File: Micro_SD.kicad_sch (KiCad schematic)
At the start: 3 parts, among them J2 DM3BT-DSF-PEJS

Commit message: BOM update
completed the BOM list
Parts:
- C27: MANUFACTURER (none) -> Murata Electronics; MANUFACTURER_PART_NUMBER (none) -> GCM155R71H104KE02D
- C33: MANUFACTURER (none) -> Murata Electronics; MANUFACTURER_PART_NUMBER (none) -> GRT155R61A105KE01D
- J2: MANUFACTURER (none) -> Hirose Electric Co Ltd; MANUFACTURER_PART_NUMBER (none) -> DM3BT-DSF-PEJS
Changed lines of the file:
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@@
+			)
+		)
+		(property "MANUFACTURER" "Murata Electronics"
+			(at 113.03 92.71 0)
+			(effects
+				(font
+					(size 1.27 1.27)
+				)
+				(hide yes)
+			)
+		)
+		(property "MANUFACTURER_PART_NUMBER" "GCM155R71H104KE02D"
+			(at 113.03 92.71 0)
+			(effects
+				(font
+					(size 1.27 1.27)
+				)
+				(hide yes)
 			)
 		)
@@
 			)
 		)
+		(property "MANUFACTURER" "Hirose Electric Co Ltd"
+			(at 128.27 69.85 0)
+			(effects
+				(font
+					(size 1.27 1.27)
+				)
+				(hide yes)
+			)
+		)
+		(property "MANUFACTURER_PART_NUMBER" "DM3BT-DSF-PEJS"
+			(at 128.27 69.85 0)
+			(effects
+				(font
+					(size 1.27 1.27)
+				)
+				(hide yes)
+			)
+		)
 		(pin "6"
 		)
@@
 			(at 124.46 92.71 0)
 			(effects
+				(font
+					(size 1.27 1.27)
+				)
+				(hide yes)
+			)
+		)
+		(property "MANUFACTURER" "Murata Electronics"
+			(at 124.46 92.71 0)
+			(effects
+				(font
+					(size 1.27 1.27)
+				)
+				(hide yes)
+			)
+		)
+		(property "MANUFACTURER_PART_NUMBER" "GRT155R61A105KE01D"
+			(at 124.46 92.71 0)
+			(effects

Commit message: Made some minor adjustments
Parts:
- C27: footprint Capacitor_SMD:C_0402_1005Metric -> Capacitor_SMD:C_0603_1608Metric
- C33: footprint Capacitor_SMD:C_0402_1005Metric -> Capacitor_SMD:C_0805_2012Metric
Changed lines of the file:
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@@
 			)
 		)
-		(property "Footprint" "Capacitor_SMD:C_0402_1005Metric"
+		(property "Footprint" "Capacitor_SMD:C_0603_1608Metric"
 			(at 113.9952 96.52 0)
 			(effects
@@
 			)
 		)
-		(property "Footprint" "Capacitor_SMD:C_0402_1005Metric"
+		(property "Footprint" "Capacitor_SMD:C_0805_2012Metric"
 			(at 125.4252 96.52 0)
 			(effects

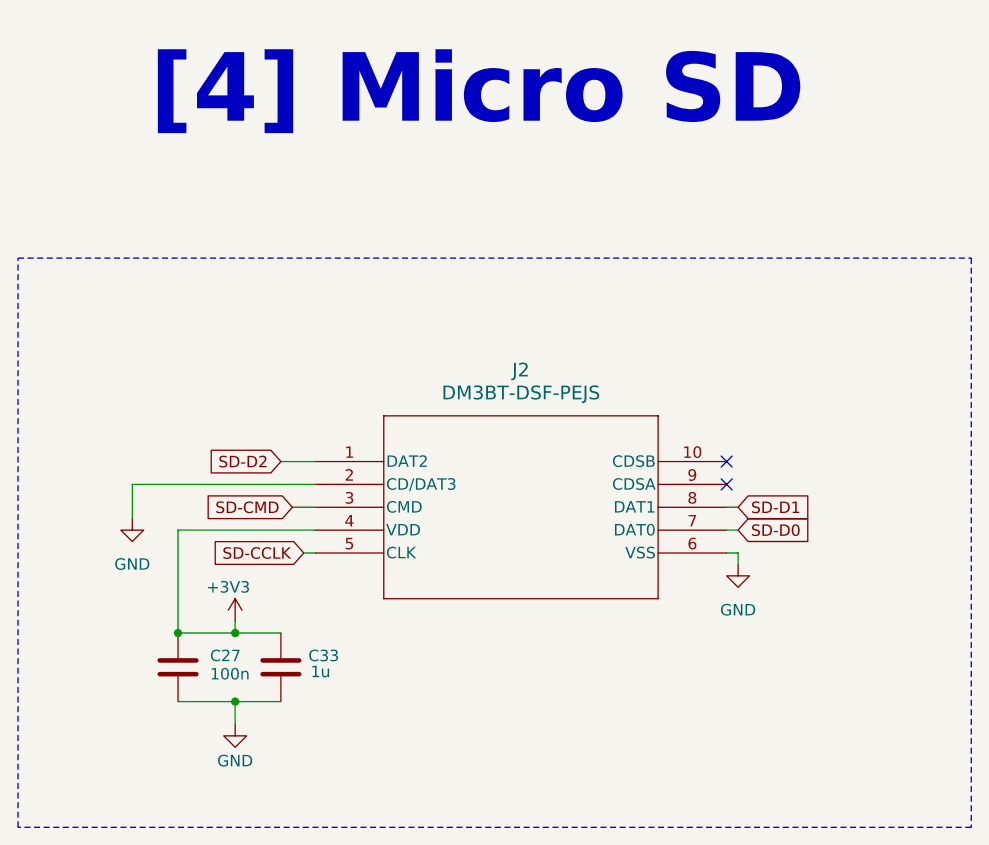
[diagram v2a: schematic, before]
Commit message: Added hierarchical lables to the schematic
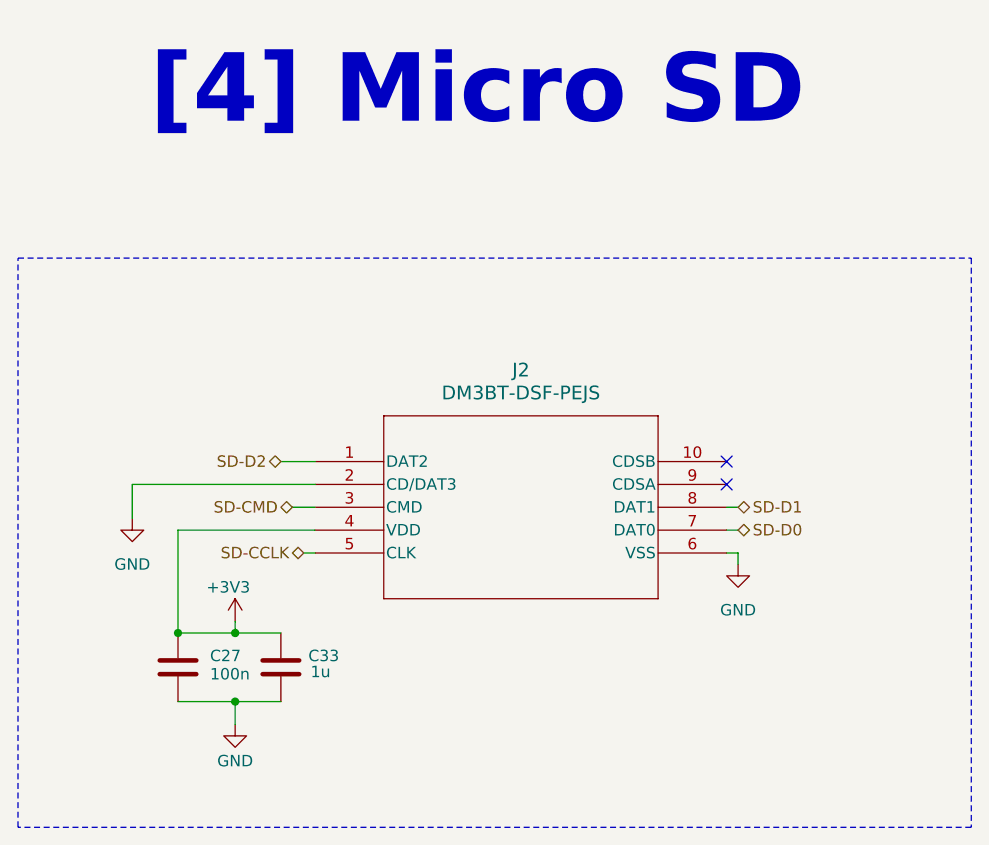
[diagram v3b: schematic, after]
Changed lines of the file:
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@@
 		)
 	)
-	(global_label "SD-CMD"
-		(shape input)
-		(at 125.73 74.93 180)
-		(fields_autoplaced yes)
+	(hierarchical_label "SD-CCLK"
+		(shape bidirectional)
+		(at 127 80.01 180)
 		(effects
 			(font
@@
 			(justify right)
 		)
-		(property "Intersheetrefs" "${INTERSHEET_REFS}"
-			(at 114.7015 74.93 0)
-			(effects
-				(font
-					(size 1.27 1.27)
-				)
-				(justify right)
-				(hide yes)
-			)
-		)
 	)
-	(global_label "SD-D0"
-		(shape input)
-		(at 175.26 77.47 0)
-		(fields_autoplaced yes)
+	(hierarchical_label "SD-D1"
+		(shape bidirectional)
+		(at 175.26 74.93 0)
 		(effects
 			(font
@@
 			(justify left)
 		)
-		(property "Intersheetrefs" "${INTERSHEET_REFS}"
-			(at 184.7766 77.47 0)
-			(effects
-				(font
-					(size 1.27 1.27)
-				)
-				(justify left)
-				(hide yes)
-			)
-		)
 	)
-	(global_label "SD-CCLK"
-		(shape input)
-		(at 127 80.01 180)
-		(fields_autoplaced yes)
+	(hierarchical_label "SD-CMD"
+		(shape bidirectional)
+		(at 125.73 74.93 180)
 		(effects
 			(font
@@
 			(justify right)
 		)
-		(property "Intersheetrefs" "${INTERSHEET_REFS}"
-			(at 115.1248 80.01 0)
-			(effects
-				(font
-					(size 1.27 1.27)
-				)
-				(justify right)
-				(hide yes)
-			)
-		)
 	)
-	(global_label "SD-D1"
-		(shape input)
-		(at 175.26 74.93 0)
-		(fields_autoplaced yes)
+	(hierarchical_label "SD-D0"
+		(shape bidirectional)
+		(at 175.26 77.47 0)
 		(effects
 			(font
@@
 			(justify left)
 		)
-		(property "Intersheetrefs" "${INTERSHEET_REFS}"
-			(at 184.7766 74.93 0)
-			(effects
-				(font
-					(size 1.27 1.27)
-				)
-				(justify left)
-				(hide yes)
-			)
-		)
 	)
-	(global_label "SD-D2"
-		(shape input)
+	(hierarchical_label "SD-D2"
+		(shape bidirectional)
 		(at 124.46 69.85 180)
-		(fields_autoplaced yes)
 		(effects
 			(font
@@
 			(justify right)
 		)
-		(property "Intersheetrefs" "${INTERSHEET_REFS}"
-			(at 114.9434 69.85 0)
-			(effects
-				(font
-					(size 1.27 1.27)
-				)
-				(justify right)
-				(hide yes)
-			)
-		)
 	)
